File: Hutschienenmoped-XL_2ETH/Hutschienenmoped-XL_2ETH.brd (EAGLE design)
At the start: 166.3 x 101.8 mm, 125 parts, among them J1 638207222005, J10 61300811821, J11 61300611821, J12 61300615721, J13 638207222005, J14 61300815721, J15 638207222008, J2 645004114822, J4 61300421121, J7 638207222005, J8 638207222007, U4 TLE9250VSJ

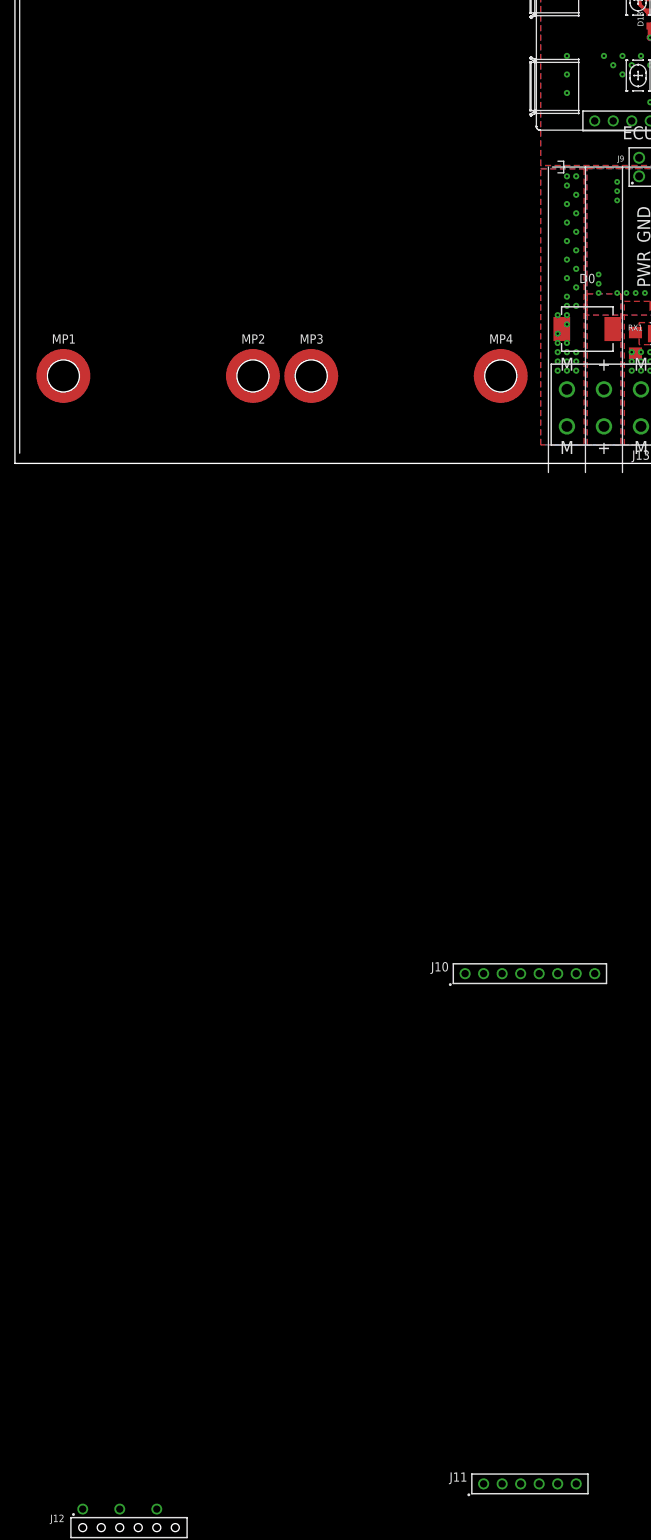
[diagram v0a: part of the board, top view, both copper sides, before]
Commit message: Update grid settings to display grid lines, add wires for a new component. Remove redundant package elements and attributes.
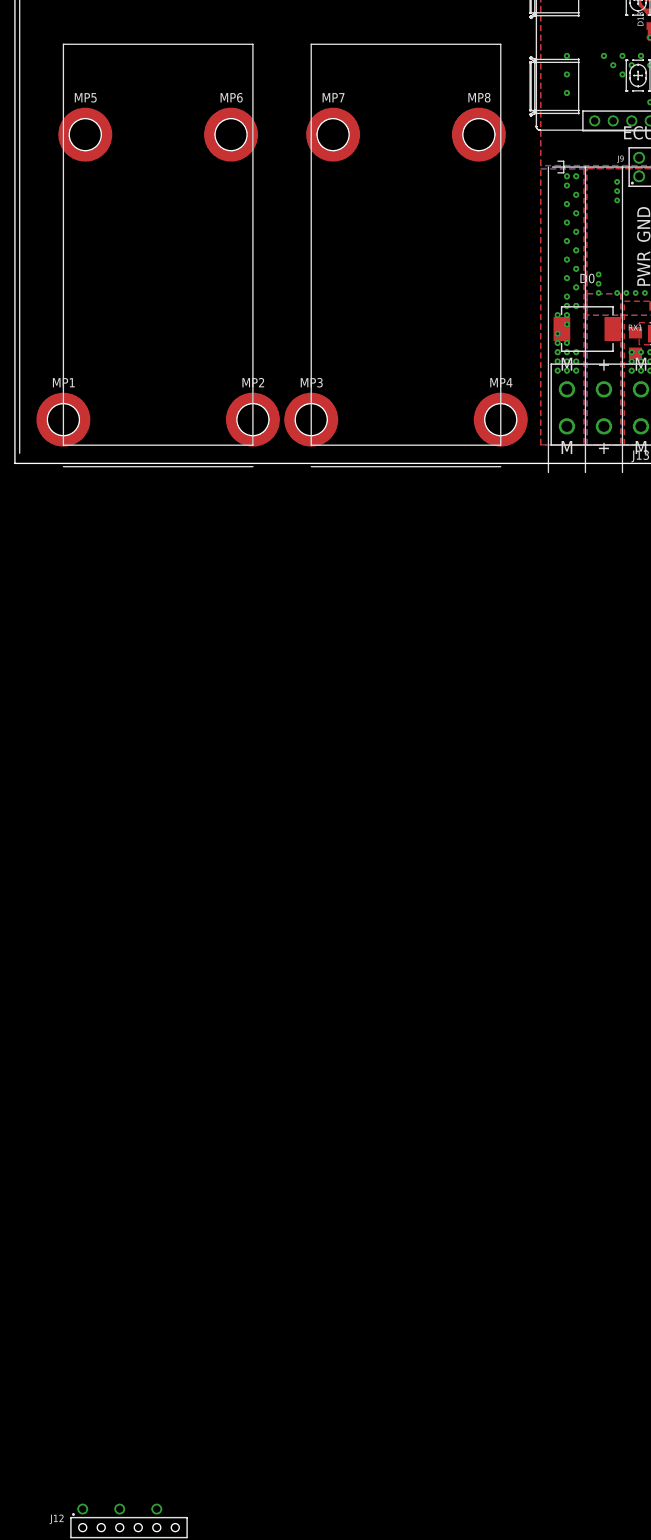
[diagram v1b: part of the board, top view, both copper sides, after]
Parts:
- removed J10: 61300811821, Wurth_Connectors_WR-PHD:61300811821
- removed J11: 61300611821, Wurth_Connectors_WR-PHD:61300611821
- added MP5, MP6, MP7, MP8: M3 x 2.5mm, Wurth_Assembly_WA-SMSI:WA-SMSI_9774025360
- moved MP1 6.00 mm to (-64.0, 6.00)
- moved MP2 6.00 mm to (-38.0, 6.00)
- moved MP3 6.00 mm to (-30.0, 6.00)
- moved MP4 6.00 mm to (-4.00, 6.00)

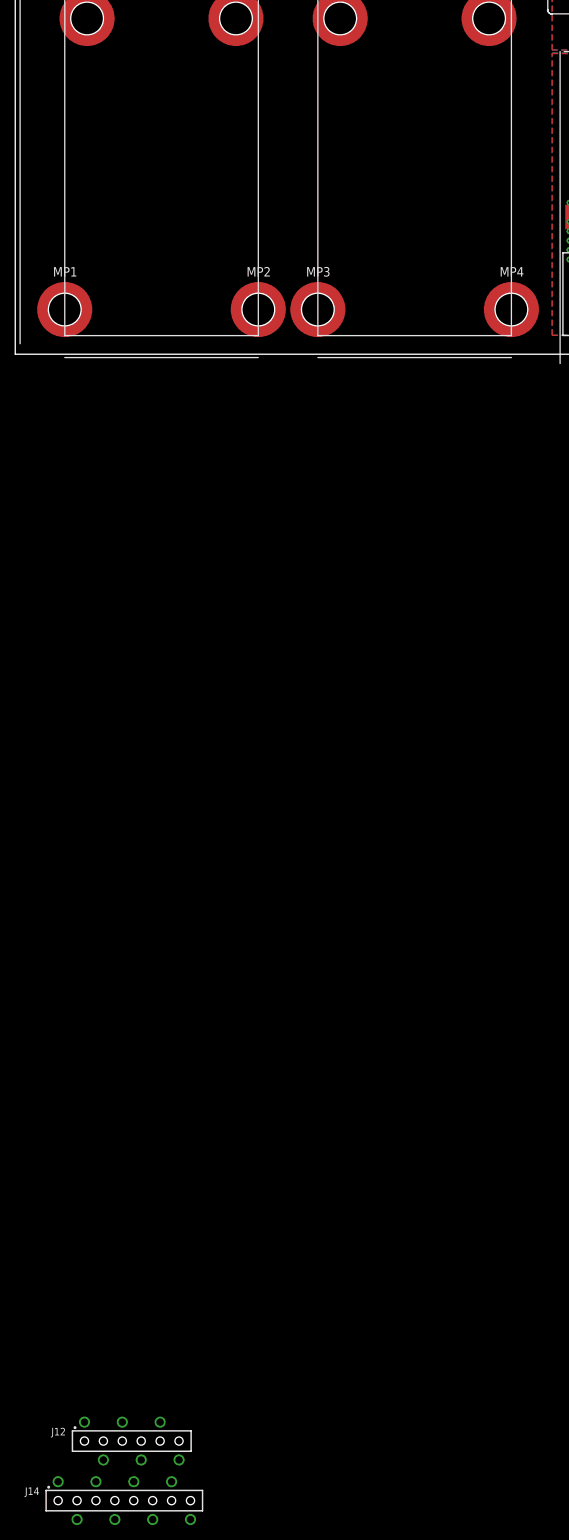
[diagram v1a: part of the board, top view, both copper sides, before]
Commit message: Update grid distance in board file and rename connector elements: - Changed grid distance from 6mm to 22.86mm for better alignment. - Renamed connector elements J12, J14 to W1-J2, W1-J1 respectively. - Added new connector elements W2-J2, W2-J1 with updated positions.
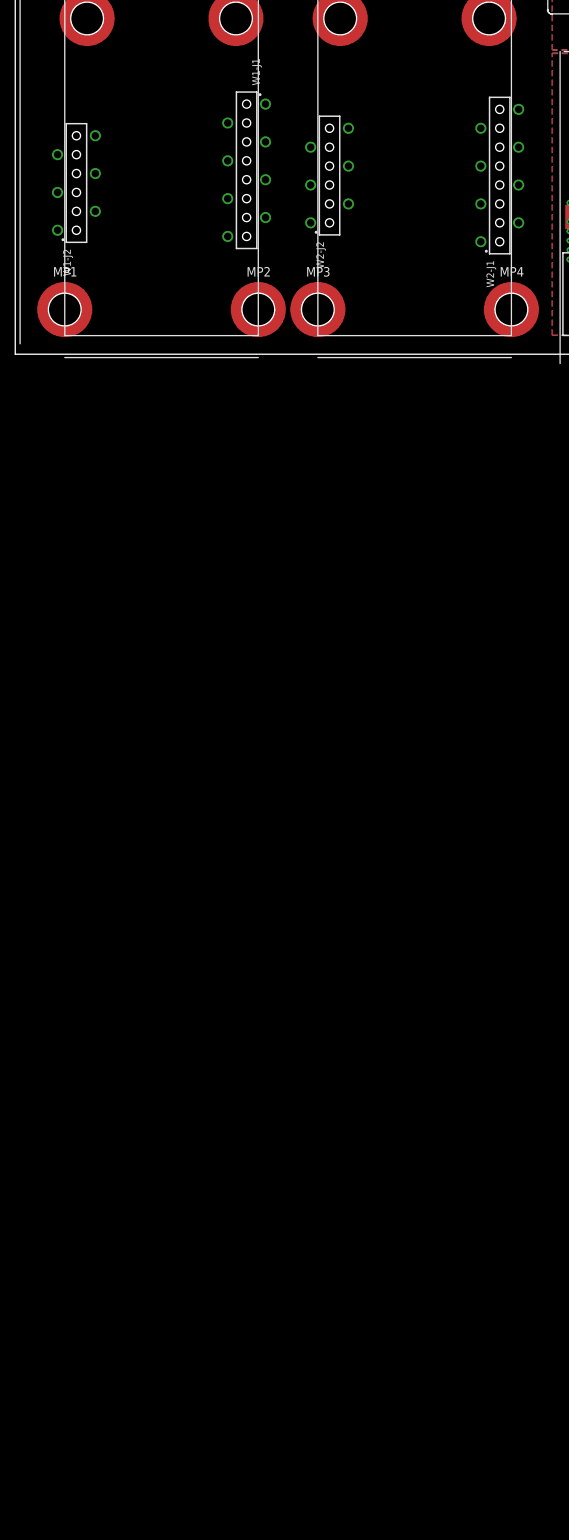
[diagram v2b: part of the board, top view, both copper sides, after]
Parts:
- removed J12: 61300615721, Wurth_Connectors_WR-PHD:61300615721
- removed J14: 61300815721, Wurth_Connectors_WR-PHD:61300815721
- added W1-J1, W2-J1: 61300815721, Wurth_Connectors_WR-PHD:61300815721
- added W1-J2, W2-J2: 61300615721, Wurth_Connectors_WR-PHD:61300615721

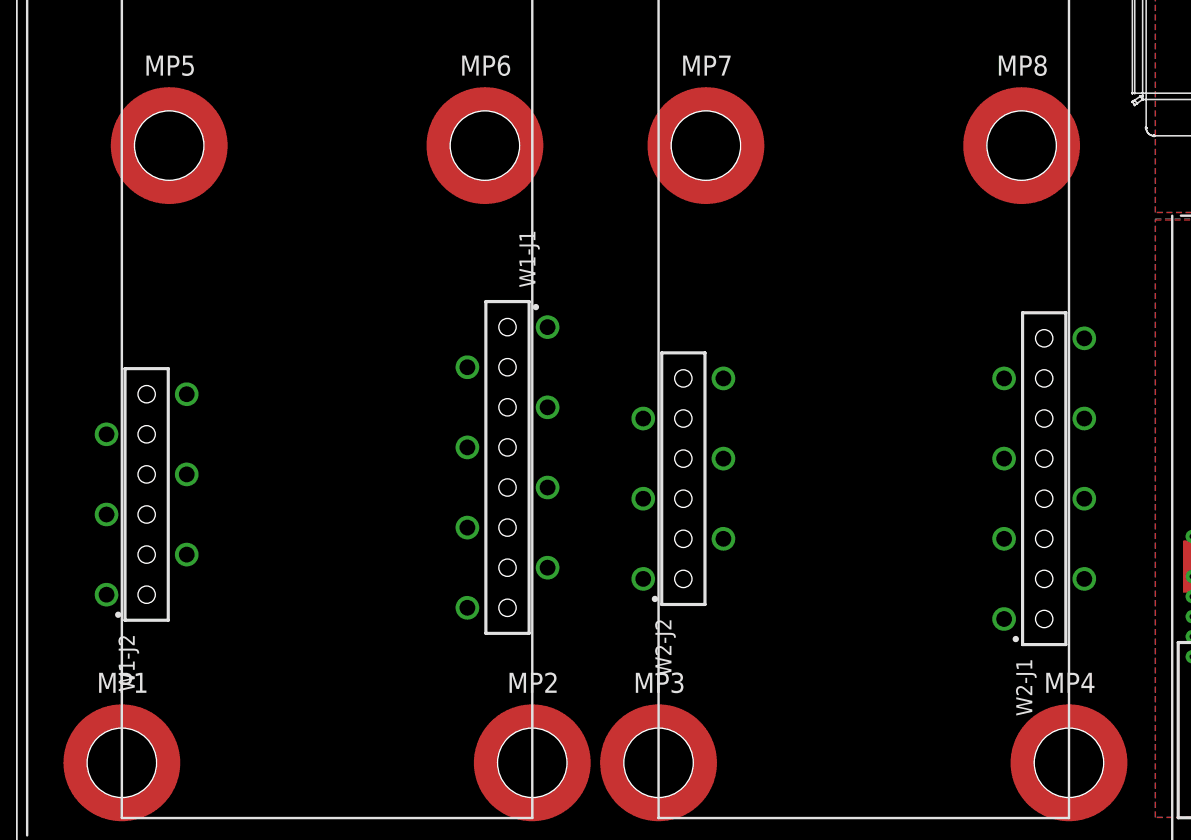
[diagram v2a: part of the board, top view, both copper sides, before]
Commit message: Update grid distance to 32.4mm, adjust connector positions.
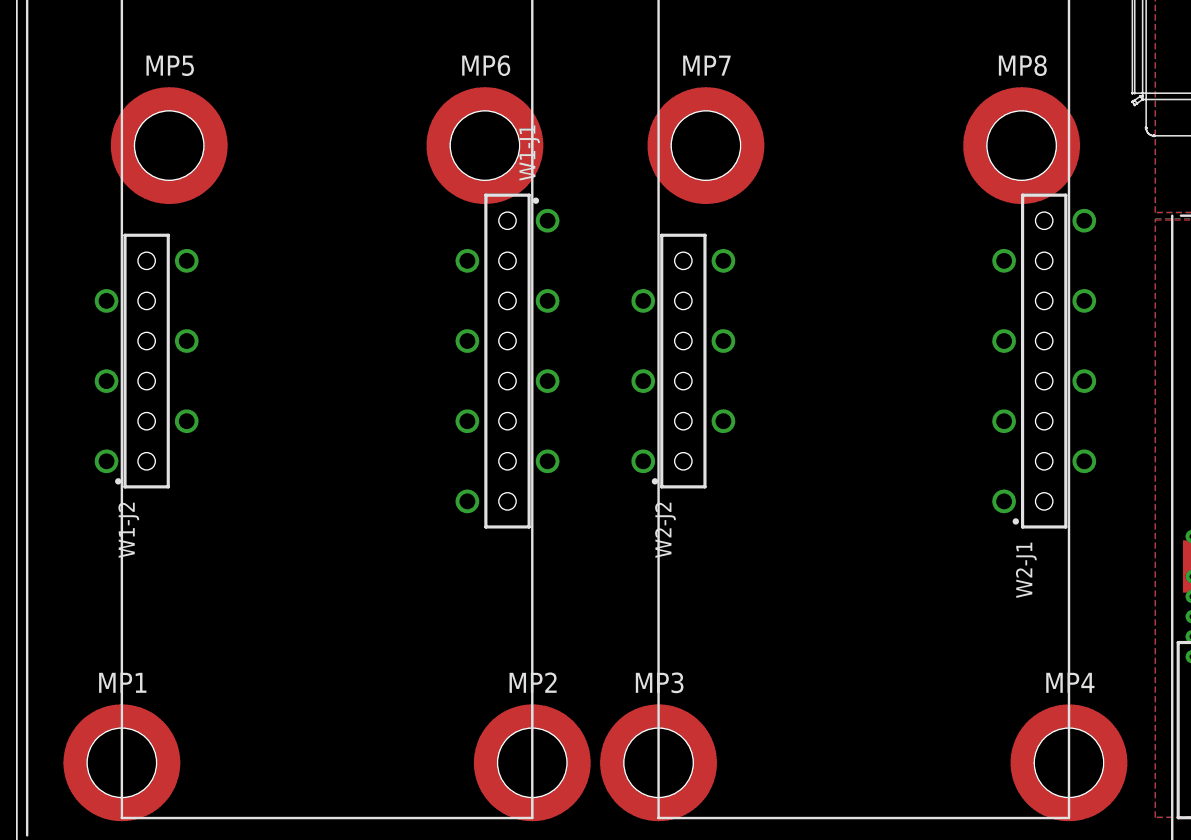
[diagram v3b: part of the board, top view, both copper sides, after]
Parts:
- moved W1-J2 8.45 mm to (-62.4, 31.4)
- moved W2-J1 7.45 mm to (-5.57, 31.4)
- moved W2-J2 7.45 mm to (-28.4, 31.4)
- moved W1-J1 6.74 mm to (-39.6, 31.4)

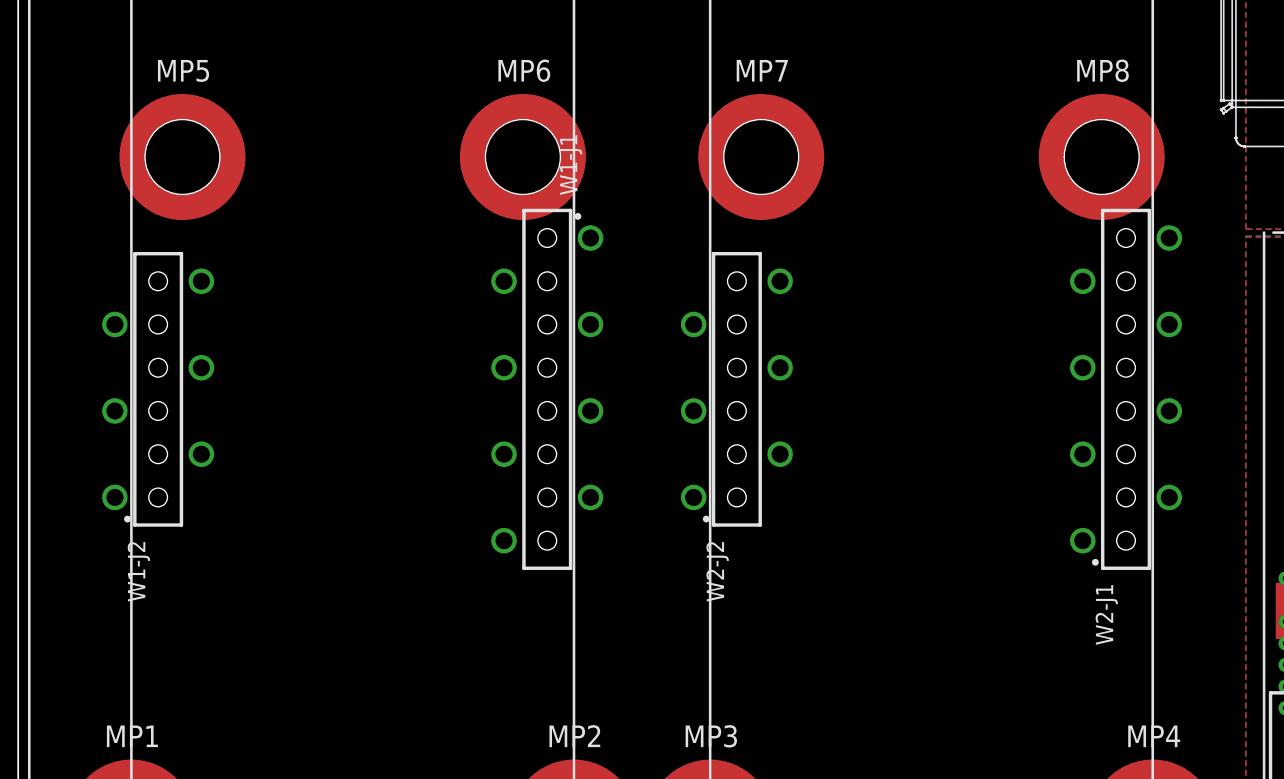
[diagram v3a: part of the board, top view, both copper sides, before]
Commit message: Update connector attributes for W1-J2 and W1-J1 elements. Fix rotation and layer settings.
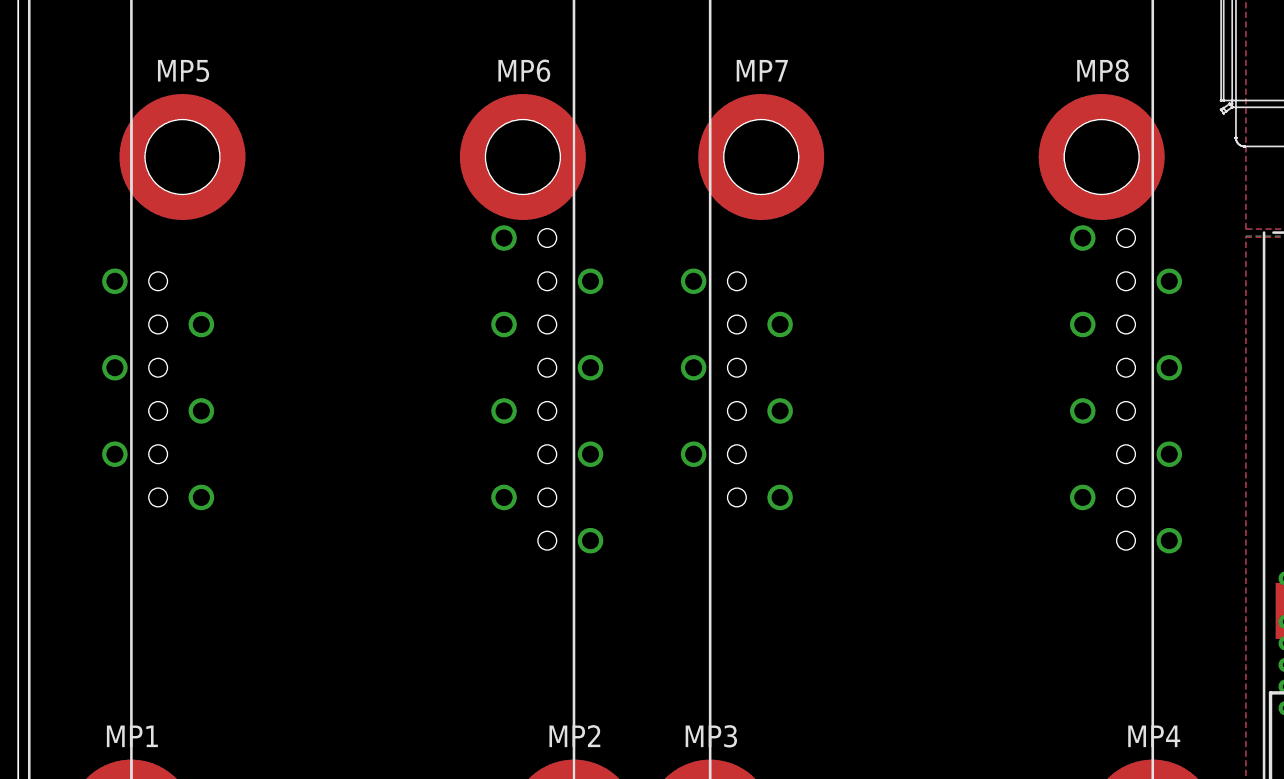
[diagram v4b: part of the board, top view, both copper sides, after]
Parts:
- flipped W1-J1 to the bottom
- flipped W1-J2 to the bottom
- flipped W2-J1 to the bottom
- flipped W2-J2 to the bottom
